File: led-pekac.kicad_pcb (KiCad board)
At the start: 2 copper layers, 186.2 x 39.4 mm, 54 parts, among them J1 Conn_01x04, J2 24V, J3 Console, J4 Pi Zero, J5 Cool, J6 Warm, J7 Conn_01x40_Female, Q1 2N7002, Q2 2N7002, Q3 IPD50N06S4L08ATMA2, Q4 IPD50N06S4L08ATMA2, SW1 Wheel, U1 SWITCHING-3TERM-5V, U2 SWITCHING-3TERM-3V3, U3 MAX6956AAX+, U4 DA56-11GWA, U5 DA56-11GWA, U6 TC1427COA, U7 MCP3426A0-E/SN

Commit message: update component values
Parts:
- C11: value 0.1uF -> 10uF Tantalum
- C8, C9: value 100n -> 100nF
- R1: value R -> 47k
- R10, R9: value R_Small -> 12.1k 0.1%
- R4, R5: value 200k -> 220k
- R6, R7, R8: value 100 -> 160

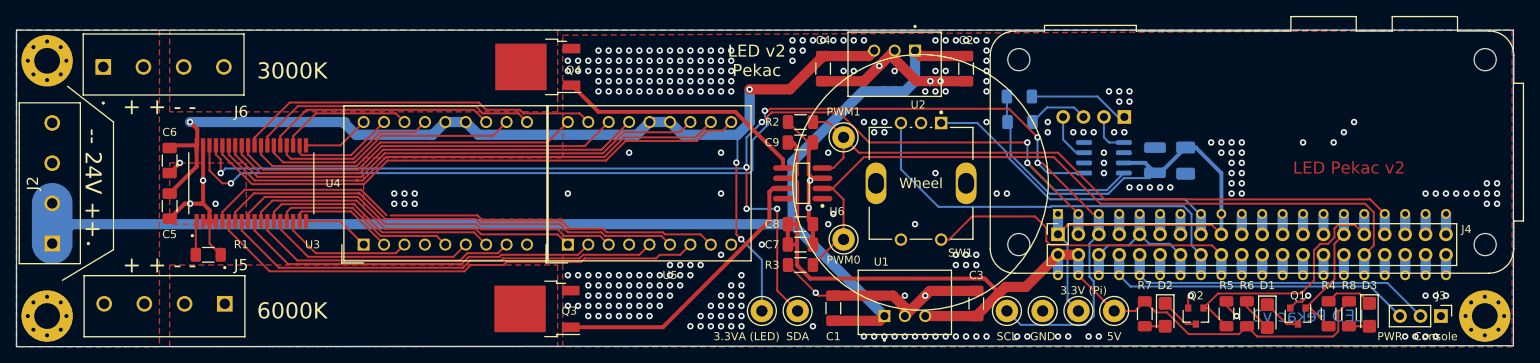
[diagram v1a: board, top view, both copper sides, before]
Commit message: Fix two serious routing bugs
The `dig4_c` trace was, unfortunately, left unconnected after my night
pour optimization (...). I had to add a fixup wire to the first
prototype.

Also, the Pi module's footprint is a bit larger than the silkscreen
because the SD card protrudes a little bit to the left, towards the
rotary encoder. I tried to make this less urgent (note that I'm
deliberately not saying "fixed") by moving the rotary encoder a bit to
the left, which necessitated moving the PWM testpoints as well, which
required some rerouting. Meh.

I think that a real fix is to leave the SD card accessible, which will
mean rotating the Pi module 180 degrees. Some other time, perhaps.
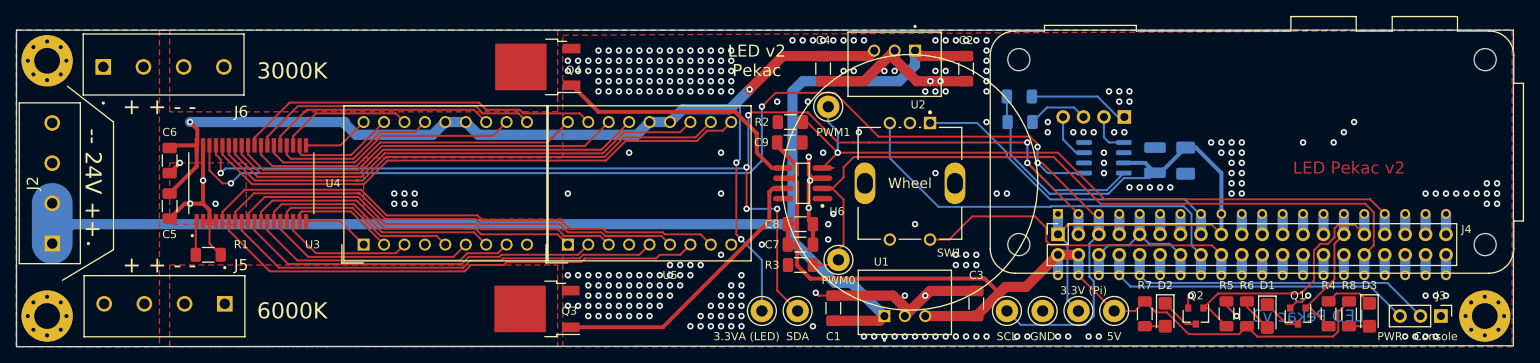
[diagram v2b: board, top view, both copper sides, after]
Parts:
- moved TP8 4.26 mm to (182.2, 70.5)
- moved TP7 2.62 mm to (183.5, 89.5)
- moved SW1 1.38 mm to (192.4, 80.0)
- moved C9 1.32 mm to (177.5, 74.9)
- moved R2 1.27 mm to (177.5, 72.4)
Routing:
- net GND: track 140.2 -> 128.8 mm, vias 304 -> 301
- net /PWM1: track 84.1 -> 89.9 mm, vias 0 -> 1
- net +24V: track 158.4 -> 163.6 mm
- net +3.3VA: track 132.7 -> 135.4 mm
- net /PWM0: track 94.5 -> 96.2 mm
- net I2C_SDA: track 161.8 -> 163.3 mm
- net I2C_SCL: track 160.9 -> 162.3 mm
- net /pi_18: track 41.5 -> 42.9 mm
- net /pi_15: track 39.8 -> 41.2 mm
- net Net-(Q4-Pad1): track 31.2 -> 32.0 mm
- net /pi_16: track 52.4 -> 52.9 mm

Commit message: wrk?
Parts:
- removed H1, H2, H3: MountingHole_3.2mm_M3_Pad_Via, MountingHole:MountingHole_3.2mm_M3_Pad_Via
- added R11: 12.1k 0.1%, Resistor_SMD:R_1206_3216Metric_Pad1.30x1.75mm_HandSolder, B.Cu at (231.1, 77.2)
- added R12: 12.1k 0.1%, Resistor_SMD:R_1206_3216Metric_Pad1.30x1.75mm_HandSolder, B.Cu at (234.3, 77.2)
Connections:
- SW1 pad 3: Net-(SW1-Pad3) -> (no net)
- SW1 pad 4: Net-(SW1-Pad4) -> (no net)
- U4 pad 4: Net-(U4-Pad4) -> (no net)
- U4 pad 9: Net-(U4-Pad9) -> (no net)
- U5 pad 4: Net-(U5-Pad4) -> (no net)
- U5 pad 9: Net-(U5-Pad9) -> (no net)
- U6 pad 1: Net-(U6-Pad1) -> (no net)
- U6 pad 8: Net-(U6-Pad8) -> (no net)
- U7 pad 2: GND -> /adc_mid
- U7 pad 8: GND -> /adc_mid
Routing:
- net /adc_mid: track 0.00 -> 22.7 mm, vias 0 -> 2
- net GND: vias 301 -> 295
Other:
- board text added: "LED Pekac v3"
- board text added: "LED v3 Pekac"
- board text removed: "LED v2 Pekac"
